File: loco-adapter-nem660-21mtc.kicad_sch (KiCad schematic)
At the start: 9 parts, among them J701 Conn_02x11_Odd_Even

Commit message: Add - Fix ERC errors
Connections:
- no-connect marks 1 -> 11
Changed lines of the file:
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@@
+	)
+	(no_connect
+		(at 26.67 80.01)
+	)
+	(no_connect
+		(at 26.67 100.33)
+	)
+	(no_connect
+		(at 26.67 85.09)
 	)
 	(no_connect
 		(at 53.34 105.41)
 	)
+	(no_connect
+		(at 26.67 102.87)
+	)
+	(no_connect
+		(at 26.67 87.63)
+	)
+	(no_connect
+		(at 91.44 92.71)
+	)
+	(no_connect
+		(at 91.44 97.79)
+	)
+	(no_connect
+		(at 91.44 102.87)
+	)
+	(no_connect
+		(at 91.44 100.33)
+	)
+	(no_connect
+		(at 26.67 82.55)
+	)
 	(wire
 		(pts
@@
 	(wire
 		(pts
+			(xy 66.04 97.79) (xy 91.44 97.79)
+		)
+		(stroke
+			(width 0)
+			(type default)
+		)
+	)
+	(wire
+		(pts
 			(xy 76.2 95.25) (xy 96.52 95.25)
 		)
@@
 	(wire
 		(pts
-			(xy 66.04 97.79) (xy 88.9 97.79)
-		)
-		(stroke
-			(width 0)
-			(type default)
-		)
-	)
-	(wire
-		(pts
 			(xy 96.52 77.47) (xy 96.52 95.25)
 		)
@@
 	(wire
 		(pts
-			(xy 66.04 92.71) (xy 83.82 92.71)
+			(xy 66.04 92.71) (xy 91.44 92.71)
 		)
 		(stroke
@@
 	(wire
 		(pts
-			(xy 66.04 102.87) (xy 88.9 102.87)
+			(xy 66.04 102.87) (xy 91.44 102.87)
 		)
 		(stroke
@@
 	(wire
 		(pts
-			(xy 66.04 100.33) (xy 88.9 100.33)
-		)
-		(stroke
-			(width 0)
-			(type default)
-		)
-	)
-	(wire
-		(pts
 			(xy 26.67 87.63) (xy 53.34 87.63)
 		)
@@
 	(wire
 		(pts
+			(xy 66.04 100.33) (xy 91.44 100.33)
+		)
+		(stroke
+			(width 0)
+			(type default)
+		)
+	)
+	(wire
+		(pts
 			(xy 102.87 85.09) (xy 107.95 85.09)
 		)
@@
 	(wire
 		(pts
-			(xy 76.2 82.55) (xy 83.82 82.55)
+			(xy 76.2 82.55) (xy 91.44 82.55)
 		)
 		(stroke
@@
 	(wire
 		(pts
-			(xy 76.2 80.01) (xy 83.82 80.01)
+			(xy 76.2 80.01) (xy 91.44 80.01)
 		)
 		(stroke
@@
 	)
 	(label "DCC0"
-		(at 83.82 82.55 180)
+		(at 91.44 82.55 180)
 		(effects
 			(font
@@
 	)
 	(label "AMP_AUX2"
-		(at 88.9 100.33 180)
+		(at 91.44 100.33 180)
 		(effects
 			(font
@@
 	)
 	(label "AMP_AUX1"
-		(at 88.9 97.79 180)
+		(at 91.44 97.79 180)
 		(effects
 			(font
@@
 	)
 	(label "DCC1"
-		(at 83.82 80.01 180)
+		(at 91.44 80.01 180)
 		(effects
 			(font
@@
 	)
 	(label "AUX5"
-		(at 83.82 92.71 180)
+		(at 91.44 92.71 180)
 		(effects
 			(font
@@
 	)
 	(label "AMP_AUX3"
-		(at 88.9 102.87 180)
-		(effects
-			(font
+		(at 91.44 102.87 180)
+		(effects
+			(font

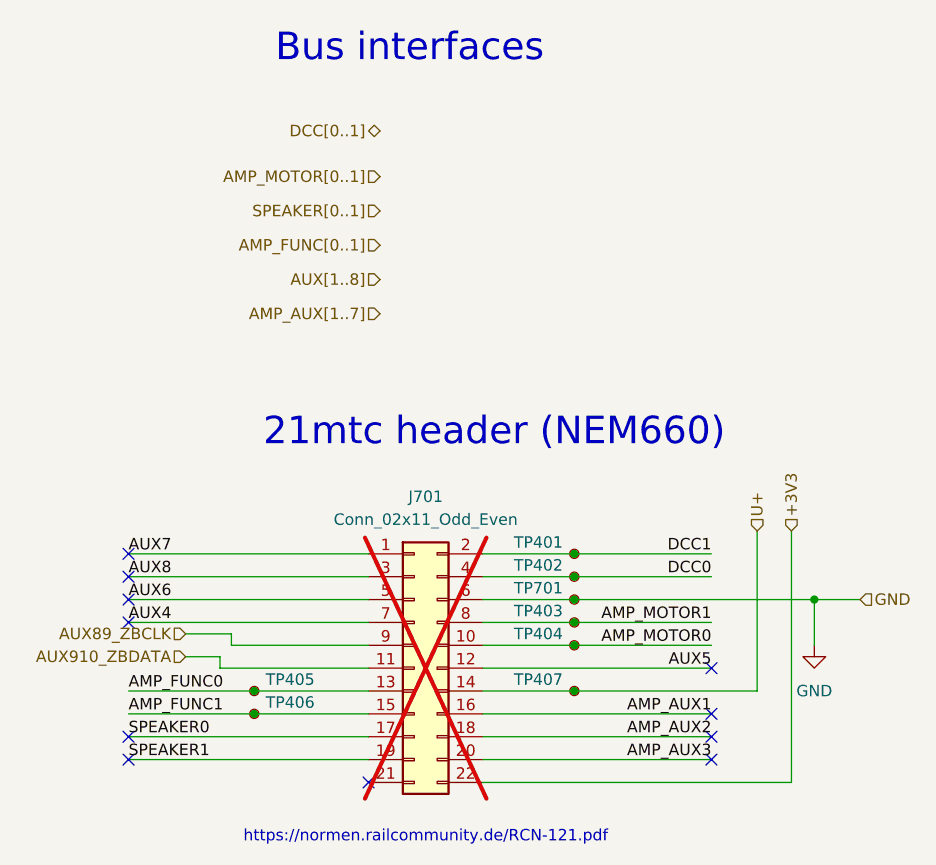
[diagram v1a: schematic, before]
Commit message: Fix - BOM errors
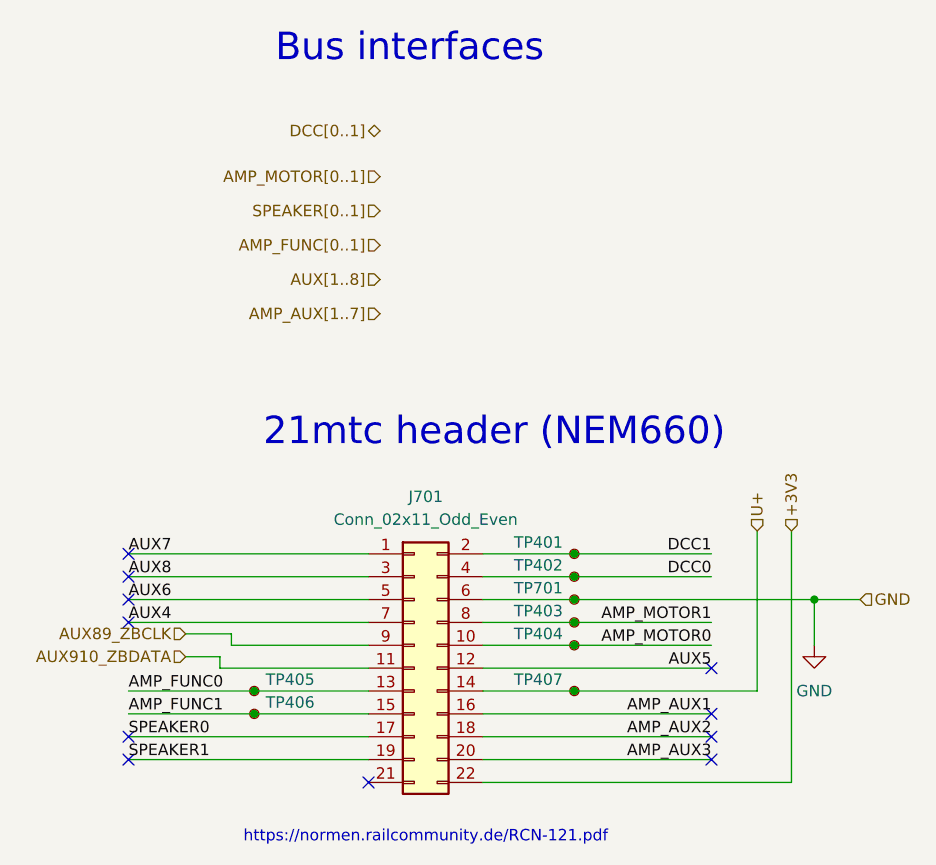
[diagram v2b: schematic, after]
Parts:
- J701: OLI_ID (none) -> MTC21_02x11_1.27; now fitted
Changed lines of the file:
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@@
 		(in_bom yes)
 		(on_board yes)
-		(dnp yes)
+		(dnp no)
 		(fields_autoplaced yes)
 		(property "Reference" "J701"
@@
 			(at 58.42 92.71 0)
 			(effects
+				(font
+					(size 1.27 1.27)
+				)
+				(hide yes)
+			)
+		)
+		(property "OLI_ID" "MTC21_02x11_1.27"
+			(at 58.42 92.71 0)
+			(effects

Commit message: Chg - Draft of Plux16 connector
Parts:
- removed TP401, TP402, TP403, TP404, TP405, TP406, TP407, TP701: ~, TestPoint:TestPoint_Pad_D1.0mm, symbol Connector:TestPoint_Small
- J?: renamed from J701; OLI_ID MTC21_02x11_1.27 -> (none); now not fitted; now left out of the parts list
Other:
- company: Chatelain Engineering, Bern - CH -> (none)
- title: xDuinoRail - RailcomDecoder - Development Kit "Hermes" -> (none)

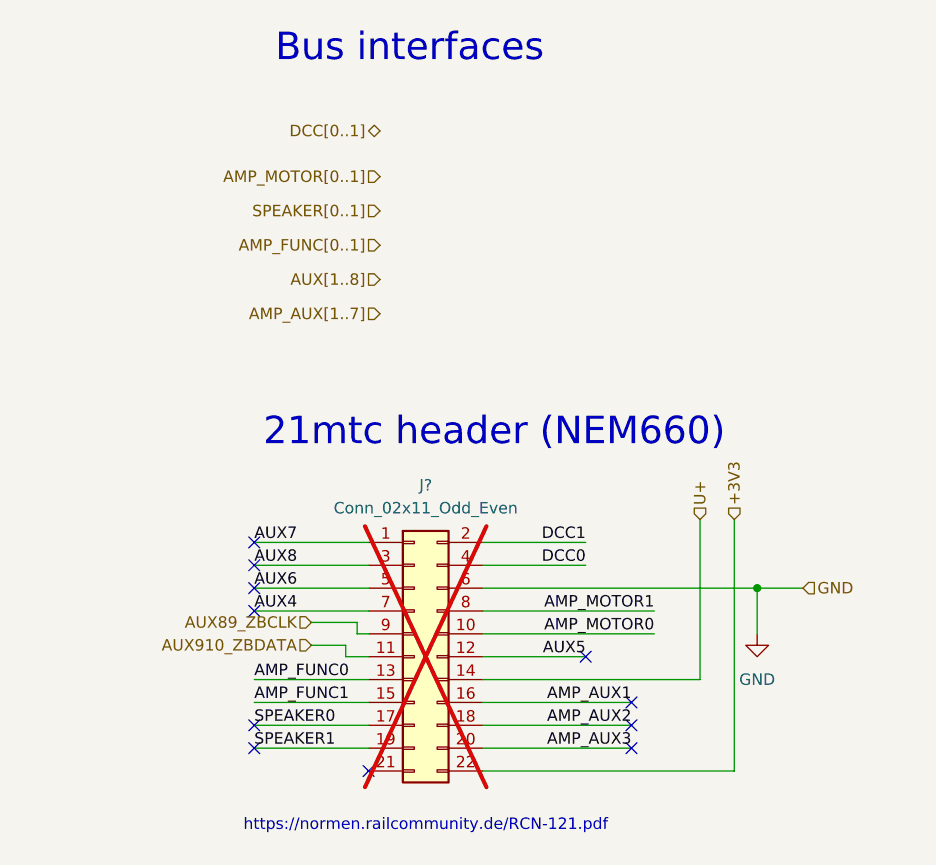
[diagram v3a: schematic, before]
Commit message: Add - New annotations of schematics
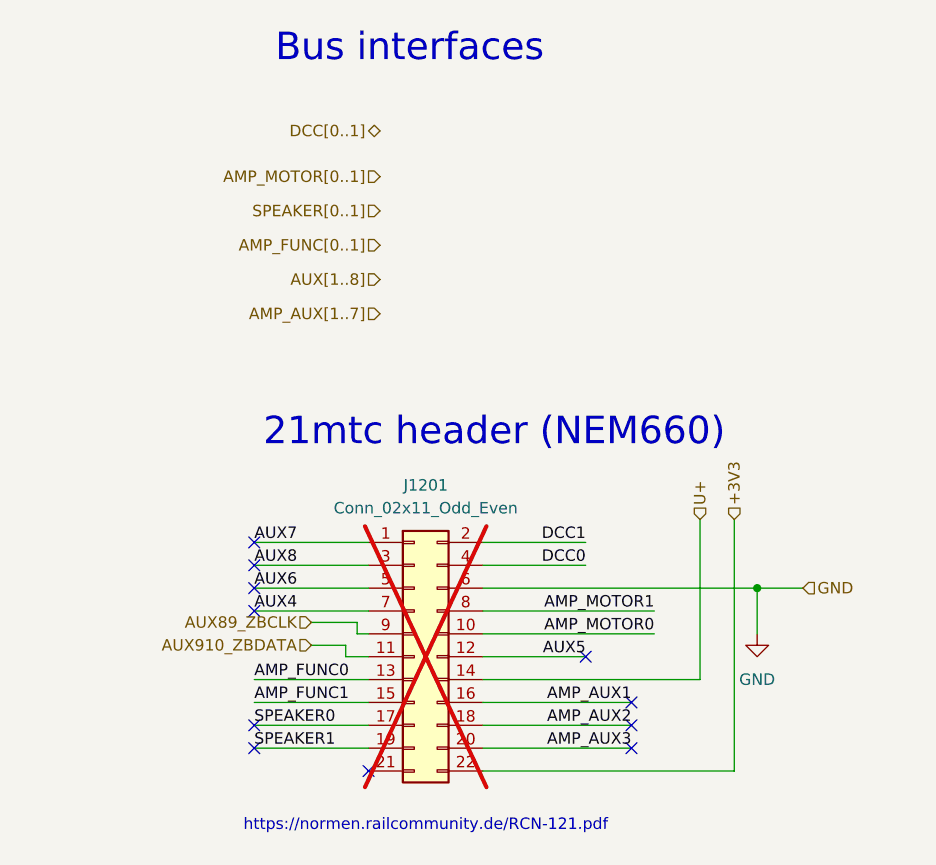
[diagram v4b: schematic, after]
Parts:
- gave numbers to parts that had none: 1
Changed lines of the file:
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@@
 		(dnp yes)
 		(fields_autoplaced yes)
-		(property "Reference" "J?"
+		(property "Reference" "J1201"
 			(at 59.69 72.39 0)
 			(effects
@@
 			(project "xDuinoRails-Thor-M"
 				(path "/fb33ec4e-6596-45d2-a121-8d3475acd69a/3c699e35-5808-46af-b922-4c3eb1f6da5c/e97feae1-09c7-4701-94c7-8bf13d7a2208"
-					(reference "J?")
+					(reference "J1201")
 					(unit 1)
 				)
@@
 		(dnp no)
 		(fields_autoplaced yes)
-		(property "Reference" "#PWR?"
+		(property "Reference" "#PWR1201"
 			(at 96.52 95.25 0)
 			(effects
@@
 			(project "xDuinoRails-Thor-M"
 				(path "/fb33ec4e-6596-45d2-a121-8d3475acd69a/3c699e35-5808-46af-b922-4c3eb1f6da5c/e97feae1-09c7-4701-94c7-8bf13d7a2208"
-					(reference "#PWR?")
+					(reference "#PWR1201")
 					(unit 1)
 				)

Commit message: Add - plux16 integration v0.9
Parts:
- added TP401, TP402, TP403, TP404, TP405, TP406, TP407, TP408: ~, TestPoint:TestPoint_Pad_D1.0mm, symbol Connector:TestPoint_Small
- J701: renamed from J1201; OLI_ID (none) -> MTC21_02x11_1.27
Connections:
- net AMP_FUNC0: now also TP406.1
- net AMP_FUNC1: now also TP408.1
- net AMP_MOTOR0: now also TP405.1
- net AMP_MOTOR1: now also TP404.1
- net DCC0: now also TP402.1
- net DCC1: now also TP401.1
- net GND: now also TP403.1
- net U+: now also TP407.1
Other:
- company: (none) -> Chatelain Engineering, Bern - CH
- title: (none) -> xDuinoRail - RailcomDecoder - Development Kit "Hermes"
- moved on the sheet: J701
